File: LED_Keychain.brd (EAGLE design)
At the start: 160 x 100 mm, 1 part

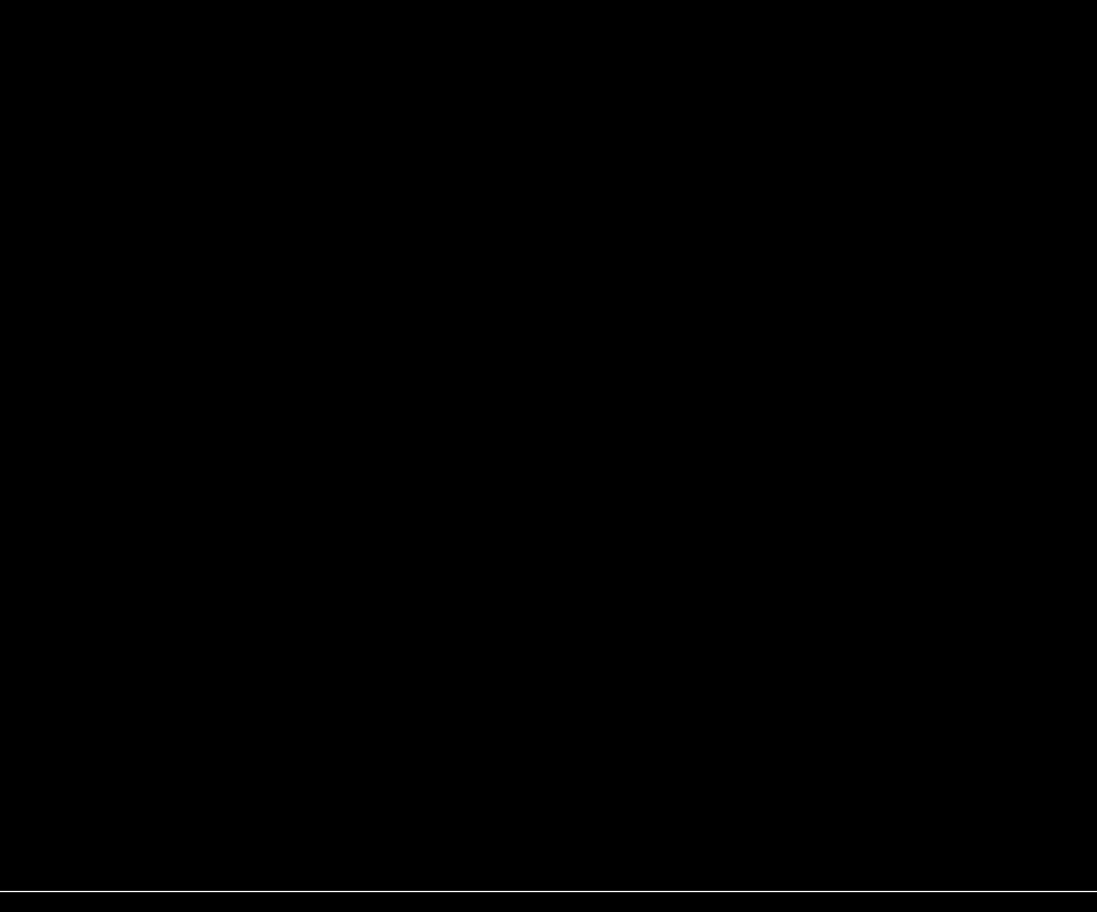
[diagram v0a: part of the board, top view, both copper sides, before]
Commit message: Added Keystone3035 in LED_Keychain_lib.lbr.
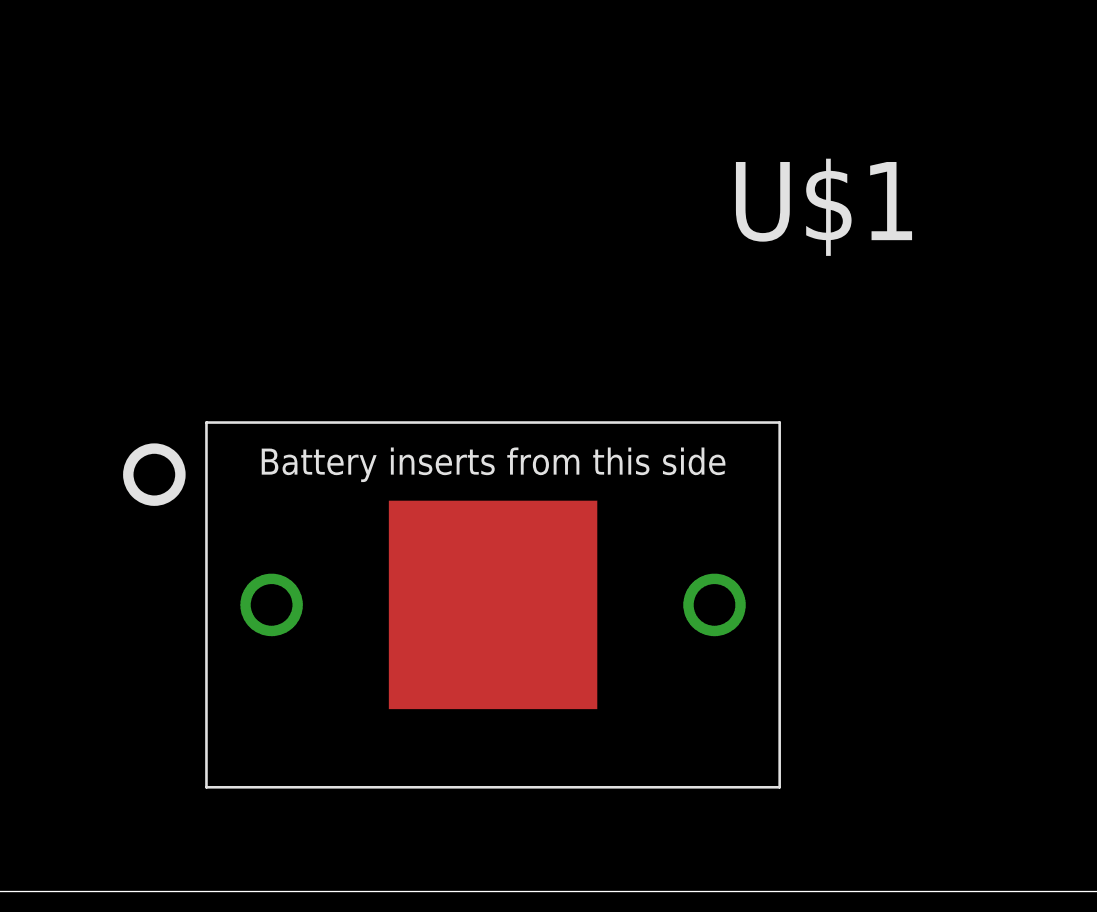
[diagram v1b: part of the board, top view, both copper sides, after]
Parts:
- added U$1: KEYSTONE3035, LED_Keychain_lib:KEYSTONE3035
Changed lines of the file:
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@@
 <attribute name="NAME" x="7.62" y="-25.66" size="1" layer="22" font="vector" ratio="13" rot="MR0" align="center"/>
+</element>
+<element name="U$1" library="LED_Keychain_lib" package="KEYSTONE3035" value="KEYSTONE3035" x="52.07" y="13.97" smashed="yes">
+<attribute name="NAME" x="63.5" y="31.75" size="3.81" layer="25"/>
 </element>
 </elements>

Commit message: Added Datasheet and made board changes
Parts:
- moved U$2 38.6 mm to (25.4, 11.4)
- moved U$1 37.7 mm to (25.4, 40.6), flipped to the bottom
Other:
- board size 160 x 100 mm -> 50.8 x 50.8 mm
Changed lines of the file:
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@@
 <board>
 <plain>
-<wire x1="0" y1="0" x2="160" y2="0" width="0" layer="20"/>
-<wire x1="160" y1="0" x2="160" y2="100" width="0" layer="20"/>
-<wire x1="160" y1="100" x2="0" y2="100" width="0" layer="20"/>
-<wire x1="0" y1="100" x2="0" y2="0" width="0" layer="20"/>
+<wire x1="0" y1="0" x2="50.8" y2="0" width="0" layer="20"/>
+<wire x1="50.8" y1="0" x2="50.8" y2="50.8" width="0" layer="20"/>
+<wire x1="50.8" y1="50.8" x2="0" y2="50.8" width="0" layer="20"/>
+<wire x1="0" y1="50.8" x2="0" y2="0" width="0" layer="20"/>
 </plain>
 <attributes>
@@
 </autorouter>
 <elements>
-<element name="U$2" library="Keyboard" package="MX-1U" value="KEYSWITCH-PLAIN-MX-1U" x="7.62" y="-22.86" smashed="yes">
-<attribute name="NAME" x="7.62" y="-25.66" size="1" layer="21" font="vector" ratio="13" align="center"/>
-<attribute name="NAME" x="7.62" y="-25.66" size="1" layer="22" font="vector" ratio="13" rot="MR0" align="center"/>
+<element name="U$2" library="Keyboard" package="MX-1U" value="KEYSWITCH-PLAIN-MX-1U" x="25.4" y="11.43" smashed="yes">
+<attribute name="NAME" x="25.4" y="8.63" size="1" layer="21" font="vector" ratio="13" align="center"/>
+<attribute name="NAME" x="25.4" y="8.63" size="1" layer="22" font="vector" ratio="13" rot="MR0" align="center"/>
 </element>
-<element name="U$1" library="LED_Keychain_lib" package="KEYSTONE3035" value="KEYSTONE3035" x="52.07" y="13.97" smashed="yes">
-<attribute name="NAME" x="63.5" y="31.75" size="3.81" layer="25"/>
+<element name="U$1" library="LED_Keychain_lib" package="KEYSTONE3035" value="KEYSTONE3035" x="25.4" y="40.64" smashed="yes" rot="MR0">
+<attribute name="NAME" x="13.97" y="58.42" size="3.81" layer="26" rot="MR0"/>
 </element>
 </elements>

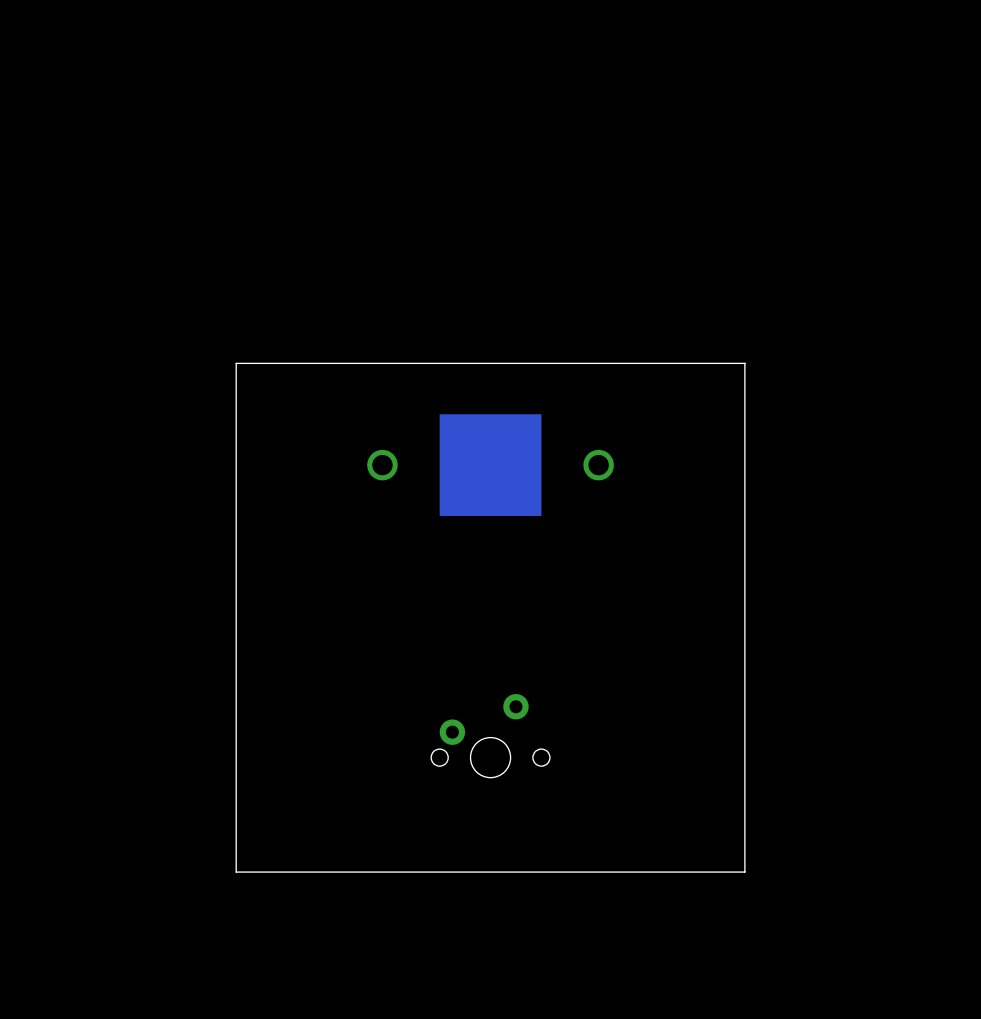
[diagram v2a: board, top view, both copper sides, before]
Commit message: Layed out the board and finished the schematic
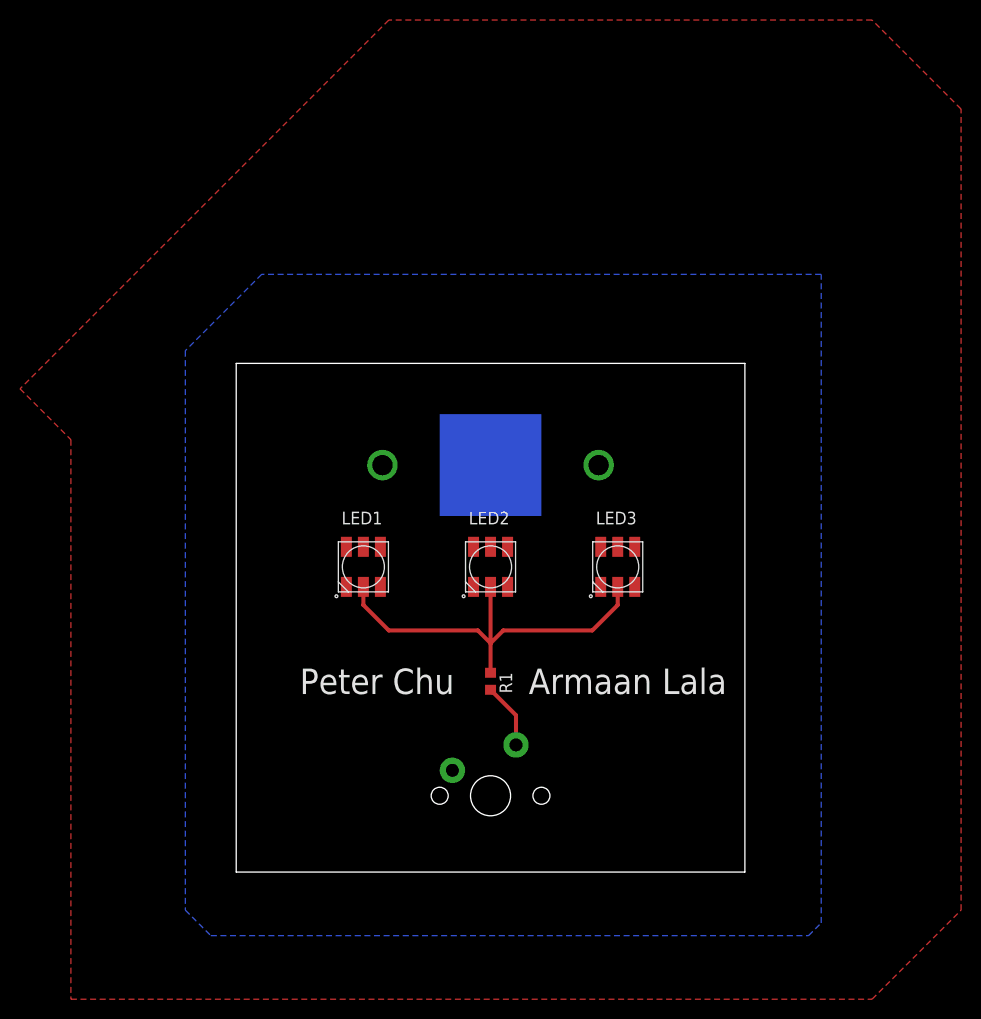
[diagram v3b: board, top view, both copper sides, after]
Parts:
- added LED1, LED2, LED3: RGBLED5050, adafruit:RGBLED5050
- added R1: (no value), adafruit:R0603
- moved U$2 3.81 mm to (25.4, 7.62)
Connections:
- new net GND: U$1.NEG, U$2.MX1
- new net LEDOUT: LED1.5, LED2.5, LED3.5, R1.1
- new net N$4: R1.2, U$2.MX2
- new net VCC: LED1.2, LED2.2, LED3.2, U$1.VCC1, U$1.VCC2
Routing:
- net LEDOUT: track 0.00 -> 40.8 mm
- net N$4: track 0.00 -> 6.55 mm
- added copper zone on layer 16, net GND
- added copper zone on layer 1, net VCC
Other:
- board text added: "Armaan Lala"
- board text added: "Peter Chu"
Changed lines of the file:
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@@
 <drawing>
 <settings>
-<setting alwaysvectorfont="no"/>
+<setting alwaysvectorfont="yes"/>
 <setting verticaltext="up"/>
 </settings>
@@
 <wire x1="50.8" y1="50.8" x2="0" y2="50.8" width="0" layer="20"/>
 <wire x1="0" y1="50.8" x2="0" y2="0" width="0" layer="20"/>
+<text x="6.35" y="17.78" size="2.54" layer="21">Peter Chu</text>
+<text x="29.21" y="17.78" size="2.54" layer="21">Armaan Lala</text>
 </plain>
 <attributes>
@@
 </autorouter>
 <elements>
-<element name="U$2" library="Keyboard" package="MX-1U" value="KEYSWITCH-PLAIN-MX-1U" x="25.4" y="11.43" smashed="yes">
-<attribute name="NAME" x="25.4" y="8.63" size="1" layer="21" font="vector" ratio="13" align="center"/>
-<attribute name="NAME" x="25.4" y="8.63" size="1" layer="22" font="vector" ratio="13" rot="MR0" align="center"/>
+<element name="U$2" library="Keyboard" package="MX-1U" value="KEYSWITCH-PLAIN-MX-1U" x="25.4" y="7.62" smashed="yes">
+<attribute name="NAME" x="25.4" y="4.82" size="1" layer="21" font="vector" ratio="13" align="center"/>
+<attribute name="NAME" x="25.4" y="4.82" size="1" layer="22" font="vector" ratio="13" rot="MR0" align="center"/>
 </element>
 <element name="U$1" library="LED_Keychain_lib" package="KEYSTONE3035" value="KEYSTONE3035" x="25.4" y="40.64" smashed="yes" rot="MR0">
 <attribute name="NAME" x="13.97" y="58.42" size="3.81" layer="26" rot="MR0"/>
 </element>
+<element name="LED1" library="adafruit" package="RGBLED5050" value="RGBLED5050" x="12.7" y="30.48" smashed="yes" rot="R270">
+<attribute name="NAME" x="10.52" y="34.72" size="1.27" layer="25" font="vector"/>
+<attribute name="VALUE" x="8.16" y="25.11" size="1.27" layer="27" font="vector"/>
+</element>
+<element name="R1" library="adafruit" package="R0603" value="" x="25.4" y="19.05" smashed="yes" rot="R270">
+<attribute name="NAME" x="26.289" y="19.939" size="1.27" layer="25" rot="R270"/>
+<attribute name="VALUE" x="23.368" y="19.939" size="1.27" layer="27" rot="R270"/>
+</element>
+<element name="LED2" library="adafruit" package="RGBLED5050" value="RGBLED5050" x="25.4" y="30.48" smashed="yes" rot="R270">
+<attribute name="NAME" x="23.22" y="34.72" size="1.27" layer="25" font="vector"/>
+<attribute name="VALUE" x="20.86" y="25.11" size="1.27" layer="27" font="vector"/>
+</element>
+<element name="LED3" library="adafruit" package="RGBLED5050" value="RGBLED5050" x="38.1" y="30.48" smashed="yes" rot="R270">
+<attribute name="NAME" x="35.92" y="34.72" size="1.27" layer="25" font="vector"/>
+<attribute name="VALUE" x="33.56" y="25.11" size="1.27" layer="27" font="vector"/>
+</element>
 </elements>
 <signals>
+<signal name="GND">
+<contactref element="U$1" pad="NEG"/>
+<contactref element="U$2" pad="MX1"/>
+<polygon width="0.1524" layer="16">
+<vertex x="-5.08" y="52.07"/>
+<vertex x="-5.08" y="-3.81"/>
+<vertex x="-2.54" y="-6.35"/>
+<vertex x="57.15" y="-6.35"/>
+<vertex x="58.42" y="-5.08"/>
+<vertex x="58.42" y="59.69"/>
+<vertex x="2.54" y="59.69"/>
+</polygon>
+</signal>
+<signal name="N$4">
+<contactref element="R1" pad="2"/>
+<contactref element="U$2" pad="MX2"/>
+<wire x1="25.4" y1="18.2" x2="27.94" y2="15.66" width="0.4064" layer="1"/>
+<wire x1="27.94" y1="15.66" x2="27.94" y2="12.7" width="0.4064" layer="1"/>
+</signal>
+<signal name="VCC">
+<contactref element="U$1" pad="VCC1"/>
+<contactref element="U$1" pad="VCC2"/>
+<contactref element="LED1" pad="2"/>
+<contactref element="LED2" pad="2"/>
+<contactref element="LED3" pad="2"/>
+<polygon width="0.1524" layer="1">
+<vertex x="-21.59" y="48.26"/>
+<vertex x="-16.51" y="43.18"/>
+<vertex x="-16.51" y="-12.7"/>
+<vertex x="63.5" y="-12.7"/>
+<vertex x="72.39" y="-3.81"/>
+<vertex x="72.39" y="76.2"/>
+<vertex x="63.5" y="85.09"/>
+<vertex x="15.24" y="85.09"/>
+</polygon>
+</signal>
+<signal name="LEDOUT">
+<contactref element="R1" pad="1"/>
+<contactref element="LED1" pad="5"/>
+<contactref element="LED2" pad="5"/>
+<contactref element="LED3" pad="5"/>
+<wire x1="12.7" y1="28.48" x2="12.7" y2="26.67" width="0.4064" layer="1"/>
+<wire x1="12.7" y1="26.67" x2="15.24" y2="24.13" width="0.4064" layer="1"/>
+<wire x1="15.24" y1="24.13" x2="24.13" y2="24.13" width="0.4064" layer="1"/>
+<wire x1="24.13" y1="24.13" x2="25.4" y2="22.86" width="0.4064" layer="1"/>
+<wire x1="25.4" y1="22.86" x2="25.4" y2="19.9" width="0.4064" layer="1"/>
+<wire x1="38.1" y1="28.48" x2="38.1" y2="26.67" width="0.4064" layer="1"/>
+<wire x1="38.1" y1="26.67" x2="35.56" y2="24.13" width="0.4064" layer="1"/>
+<wire x1="35.56" y1="24.13" x2="26.67" y2="24.13" width="0.4064" layer="1"/>
+<wire x1="26.67" y1="24.13" x2="25.4" y2="22.86" width="0.4064" layer="1"/>
+<wire x1="25.4" y1="28.48" x2="25.4" y2="22.86" width="0.4064" layer="1"/>
+</signal>
 </signals>
 <mfgpreviewcolors>
@@
 <mfgpreviewcolor name="substratecolor" color="0xFF786E46"/>
 </mfgpreviewcolors>
+<errors>
+</errors>
 </board>
 </drawing>
